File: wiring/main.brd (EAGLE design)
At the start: 75.9 x 73.7 mm, 48 parts, among them IC1 attiny 2313A, J1 J7MM, J11 J7MM, J2 J5MM, J3 J10MM, J4 J7MM, J5 J5MM, J6 J5MM, Q1 12MHz, X1 USB-B

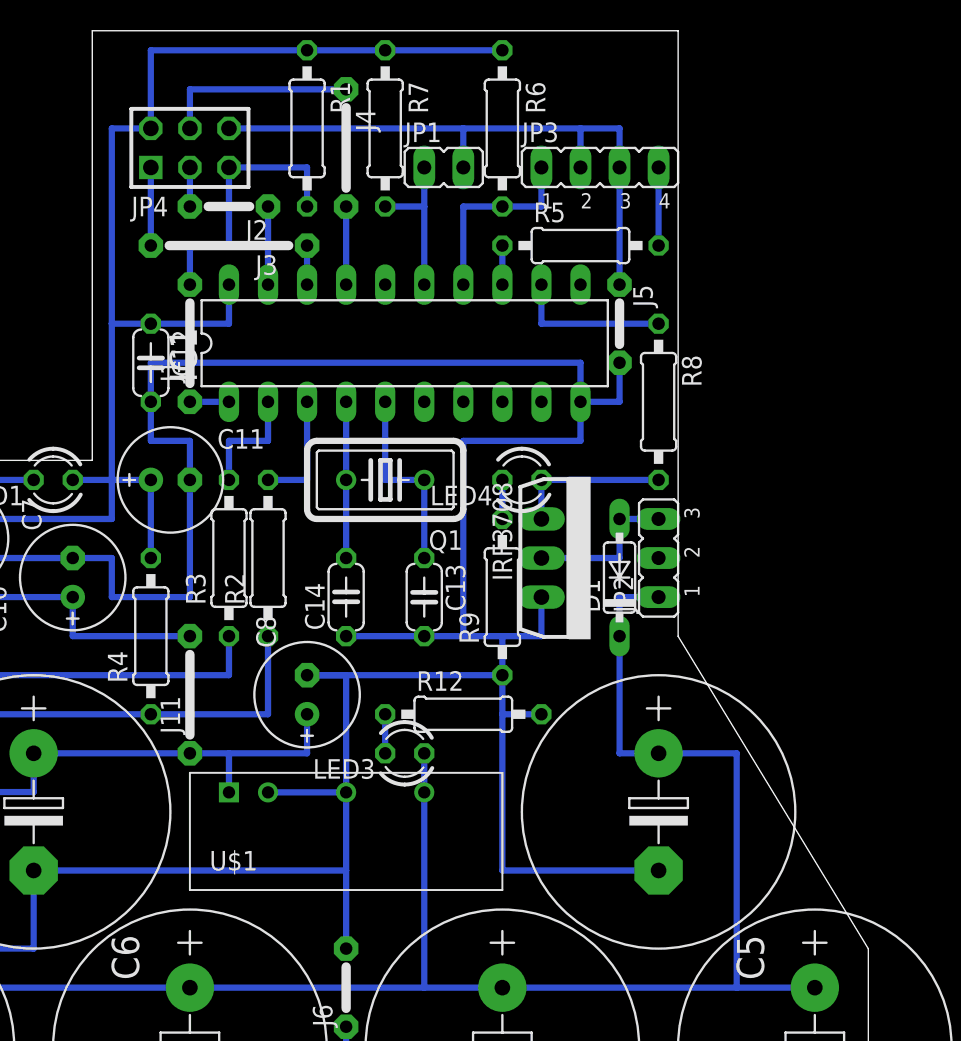
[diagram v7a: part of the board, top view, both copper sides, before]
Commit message: wiring schaltazeige led Widerstand geändert
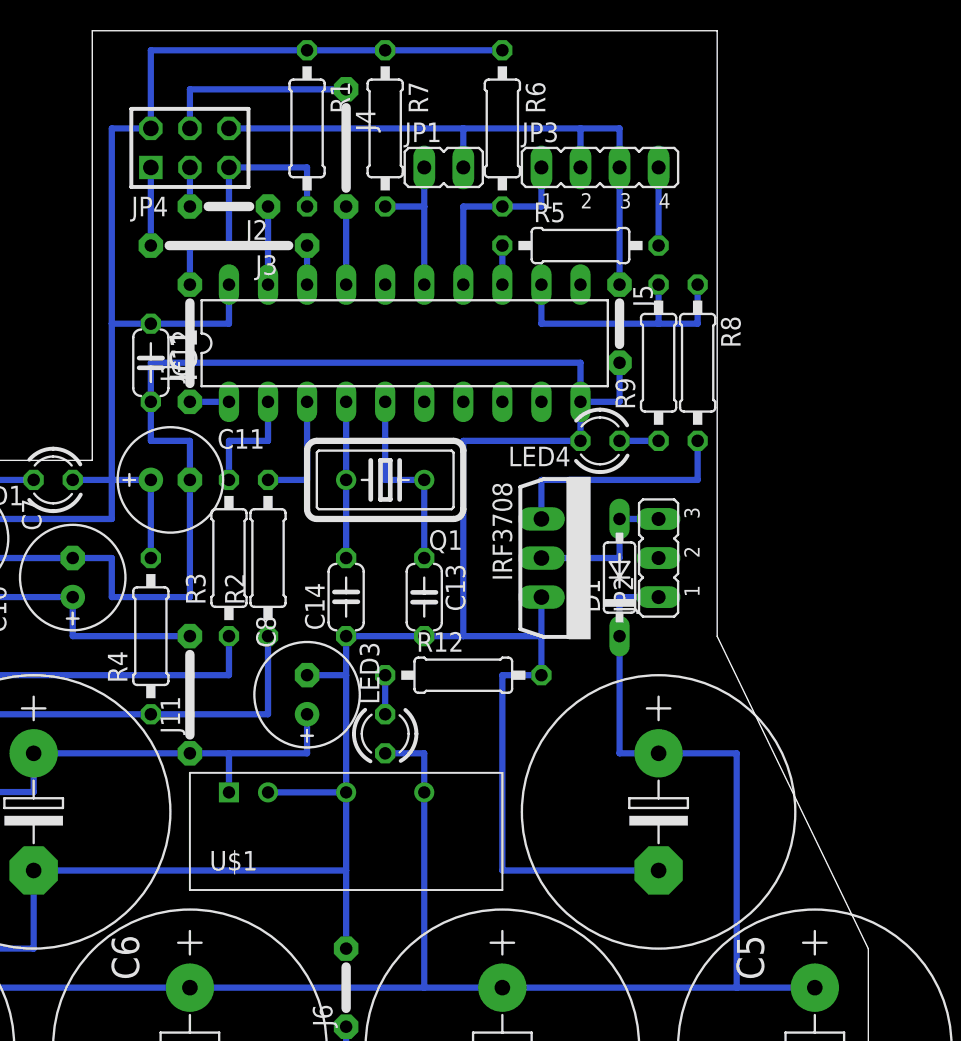
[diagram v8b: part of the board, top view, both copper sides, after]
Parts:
- R9: value 549 -> 649
- moved R9 18.3 mm to (63.5, 53.3)
- moved LED4 5.68 mm to (59.7, 48.3)
- moved R8 3.59 mm to (66.0, 53.3)
- moved R12 2.54 mm to (50.8, 33.0)
- moved LED3 1.80 mm to (45.7, 29.2), turned to 90 degrees
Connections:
- removed net N$6: LED4.K, R9.2
- new net N$7: LED4.A, R9.1
- net GND: now also LED4.K; no longer R9.1
- net N$2: no longer LED4.A
- net PB0: now also R9.2
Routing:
- net GND: track 404.0 -> 393.9 mm
- net PB0: track 10.2 -> 17.8 mm
- net N$2: track 10.2 -> 15.2 mm
- net N$7: track 0.00 -> 2.54 mm
- net N$6: track 2.54 -> 0.00 mm
- net +15V: track 111.8 -> 114.3 mm
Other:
- outline, holes or cut-outs redrawn
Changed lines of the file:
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@@
 <wire x1="1.27" y1="1.27" x2="77.14" y2="1.27" width="0" layer="20"/>
 <wire x1="77.14" y1="1.27" x2="77.14" y2="15.23" width="0" layer="20"/>
-<wire x1="77.14" y1="15.23" x2="64.77" y2="35.55" width="0" layer="20"/>
-<wire x1="64.77" y1="35.55" x2="64.77" y2="74.93" width="0" layer="20"/>
-<wire x1="64.77" y1="74.93" x2="26.67" y2="74.93" width="0" layer="20"/>
+<wire x1="77.14" y1="15.23" x2="67.31" y2="35.55" width="0" layer="20"/>
+<wire x1="67.31" y1="35.55" x2="67.31" y2="74.93" width="0" layer="20"/>
+<wire x1="67.31" y1="74.93" x2="26.67" y2="74.93" width="0" layer="20"/>
 <wire x1="26.67" y1="74.93" x2="26.67" y2="46.99" width="0" layer="20"/>
 <wire x1="26.67" y1="46.99" x2="1.27" y2="46.99" width="0" layer="20"/>
@@
 <element name="C7" library="resistor" package="E2,5-7" value="220µ" x="25.4" y="39.37" rot="R90"/>
 <element name="C10" library="resistor" package="E2,5-7" value="220µ" x="17.78" y="41.91" rot="R270"/>
-<element name="R8" library="rcl" package="0207/10" value="100" x="63.5" y="50.8" rot="R270"/>
+<element name="R8" library="rcl" package="0207/10" value="100" x="66.04" y="53.34" rot="R270"/>
 <element name="R1" library="rcl" package="0207/10" value="10k" x="40.64" y="68.58" rot="R270"/>
 <element name="C13" library="rcl" package="C050-024X044" value="22p" x="48.26" y="38.1" rot="R270"/>
@@
 <element name="D1" library="diode" package="DO35-7" value="1N4148DO35-7" x="60.96" y="39.37" rot="R90"/>
 <element name="IRF3708" library="transistor-power" package="TO262-V" value="IRF3704L-V" x="55.88" y="40.64" rot="R270"/>
-<element name="R9" library="rcl" package="0207/10" value="549" x="53.34" y="38.1" rot="R90"/>
+<element name="R9" library="rcl" package="0207/10" value="649" x="63.5" y="53.34" rot="R90"/>
 <element name="C8" library="resistor" package="E2,5-7" value="220µ" x="40.64" y="31.75" rot="R90"/>
 <element name="U$1" library="eigene" package="SIL7" value="SIM2-0515S" x="35.56" y="25.4"/>
@@
 <element name="LED1" library="led" package="LED3MM" value="" x="24.13" y="45.72" rot="R180"/>
 <element name="LED2" library="led" package="LED3MM" value="" x="11.43" y="20.32" rot="R180"/>
-<element name="LED3" library="led" package="LED3MM" value="LED 3MM 2MA GN" x="46.99" y="27.94" rot="R180"/>
+<element name="LED3" library="led" package="LED3MM" value="LED 3MM 2MA GN" x="45.72" y="29.21" rot="R90"/>
 <element name="R10" library="rcl" package="0207/7" value="649" x="11.43" y="45.72" rot="R180"/>
 <element name="R11" library="rcl" package="0207/7" value="1,5k" x="6.35" y="17.78" rot="R180"/>
-<element name="R12" library="rcl" package="0207/10" value="6,49k" x="50.8" y="30.48"/>
-<element name="LED4" library="led" package="LED3MM" value="" x="54.61" y="45.72" rot="R180"/>
+<element name="R12" library="rcl" package="0207/10" value="6,49k" x="50.8" y="33.02"/>
+<element name="LED4" library="led" package="LED3MM" value="" x="59.69" y="48.26" rot="R180"/>
 </elements>
 <signals>
@@
 <contactref element="R8" pad="2"/>
 <contactref element="IRF3708" pad="1"/>
-<wire x1="55.88" y1="43.18" x2="55.88" y2="45.72" width="0.4064" layer="16"/>
-<wire x1="55.88" y1="45.72" x2="63.5" y2="45.72" width="0.4064" layer="16"/>
-<contactref element="LED4" pad="A"/>
-<wire x1="55.88" y1="45.72" x2="55.88" y2="43.18" width="0" layer="19" extent="1-1"/>
+<wire x1="66.04" y1="48.26" x2="66.04" y2="45.72" width="0.4064" layer="16"/>
+<wire x1="66.04" y1="45.72" x2="55.88" y2="45.72" width="0.4064" layer="16"/>
+<wire x1="55.88" y1="45.72" x2="55.88" y2="43.18" width="0.4064" layer="16"/>
 </signal>
 <signal name="+5V">
@@
 <wire x1="55.88" y1="58.42" x2="55.88" y2="55.88" width="0.4064" layer="16"/>
 <wire x1="55.88" y1="55.88" x2="63.5" y2="55.88" width="0.4064" layer="16"/>
+<wire x1="63.5" y1="55.88" x2="66.04" y2="55.88" width="0.4064" layer="16"/>
+<wire x1="66.04" y1="55.88" x2="66.04" y2="58.42" width="0.4064" layer="16"/>
+<contactref element="R9" pad="2"/>
+<wire x1="63.5" y1="58.42" x2="63.5" y2="55.88" width="0.4064" layer="16"/>
 </signal>
 <signal name="N$18">
@@
 <wire x1="58.42" y1="53.34" x2="58.42" y2="50.8" width="0.4064" layer="16"/>
 <contactref element="IRF3708" pad="3"/>
-<contactref element="R9" pad="1"/>
 <wire x1="7.62" y1="20.32" x2="7.62" y2="15.24" width="0.4064" layer="16"/>
 <wire x1="7.62" y1="15.24" x2="7.62" y2="5.08" width="0.4064" layer="16"/>
-<wire x1="53.34" y1="33.02" x2="53.34" y2="35.56" width="0.4064" layer="16"/>
-<wire x1="53.34" y1="35.56" x2="50.8" y2="35.56" width="0.4064" layer="16"/>
 <wire x1="55.88" y1="38.1" x2="55.88" y2="35.56" width="0.4064" layer="16"/>
-<wire x1="55.88" y1="35.56" x2="53.34" y2="35.56" width="0.4064" layer="16"/>
+<wire x1="55.88" y1="35.56" x2="50.8" y2="35.56" width="0.4064" layer="16"/>
 <contactref element="C8" pad="-"/>
 <contactref element="C1" pad="-"/>
@@
 <contactref element="U$1" pad="PIN4"/>
 <wire x1="63.5" y1="20.32" x2="53.34" y2="20.32" width="0.4064" layer="16"/>
-<wire x1="53.34" y1="20.32" x2="53.34" y2="30.48" width="0.4064" layer="16"/>
-<wire x1="53.34" y1="30.48" x2="53.34" y2="33.02" width="0.4064" layer="16"/>
-<wire x1="40.64" y1="33.02" x2="53.34" y2="33.02" width="0.4064" layer="16"/>
+<wire x1="53.34" y1="20.32" x2="53.34" y2="33.02" width="0.4064" layer="16"/>
 <wire x1="38.1" y1="25.4" x2="43.18" y2="25.4" width="0.4064" layer="16"/>
 <contactref element="J5" pad="1"/>
@@
 <wire x1="2.54" y1="20.32" x2="7.62" y2="20.32" width="0.4064" layer="16"/>
 <wire x1="7.62" y1="20.32" x2="7.62" y2="20.65" width="0.4064" layer="16"/>
-<wire x1="55.88" y1="30.48" x2="53.34" y2="30.48" width="0.4064" layer="16"/>
+<wire x1="55.88" y1="33.02" x2="53.34" y2="33.02" width="0.4064" layer="16"/>
 <wire x1="7.62" y1="45.72" x2="2.54" y2="45.72" width="0.4064" layer="16"/>
 <wire x1="2.54" y1="45.72" x2="2.54" y2="40.64" width="0.4064" layer="16"/>
 <wire x1="22.86" y1="20.32" x2="22.86" y2="15.24" width="0.4064" layer="16"/>
 <wire x1="22.86" y1="15.24" x2="7.62" y2="15.24" width="0.4064" layer="16"/>
+<wire x1="22.86" y1="20.32" x2="43.18" y2="20.32" width="0.4064" layer="16"/>
+<contactref element="LED4" pad="K"/>
 <wire x1="60.96" y1="53.34" x2="60.96" y2="58.42" width="0" layer="19" extent="1-1"/>
-<wire x1="43.18" y1="25.4" x2="43.18" y2="33.02" width="0" layer="19" extent="16-16"/>
-<wire x1="22.86" y1="20.32" x2="43.18" y2="20.32" width="0.4064" layer="16"/>
+<wire x1="58.42" y1="48.26" x2="50.8" y2="48.26" width="0" layer="19" extent="16-16"/>
+<wire x1="43.18" y1="25.4" x2="43.18" y2="20.32" width="0" layer="19" extent="16-16"/>
+<wire x1="43.18" y1="35.56" x2="43.18" y2="33.02" width="0.4064" layer="16"/>
+<wire x1="55.88" y1="33.02" x2="55.88" y2="35.56" width="0.4064" layer="16"/>
 </signal>
 <signal name="SCK">
@@
 <contactref element="LED3" pad="A"/>
 <wire x1="48.26" y1="25.4" x2="48.26" y2="27.94" width="0.4064" layer="16"/>
+<wire x1="48.26" y1="27.94" x2="45.72" y2="27.94" width="0.4064" layer="16"/>
 </signal>
 <signal name="D-">
@@
 <contactref element="LED3" pad="K"/>
 <contactref element="R12" pad="1"/>
-<wire x1="45.72" y1="27.94" x2="45.72" y2="30.48" width="0.4064" layer="16"/>
+<wire x1="45.72" y1="30.48" x2="45.72" y2="33.02" width="0.4064" layer="16"/>
 </signal>
 <signal name="N$4">
@@
 <wire x1="45.72" y1="73.66" x2="40.64" y2="73.66" width="0" layer="19" extent="1-1"/>
 </signal>
-<signal name="N$6">
-<contactref element="R9" pad="2"/>
-<contactref element="LED4" pad="K"/>
-<wire x1="53.34" y1="43.18" x2="53.34" y2="45.72" width="0.4064" layer="16"/>
+<signal name="N$7">
+<contactref element="R9" pad="1"/>
+<contactref element="LED4" pad="A"/>
+<wire x1="63.5" y1="48.26" x2="60.96" y2="48.26" width="0.4064" layer="16"/>
 </signal>
 </signals>
-<errors>
-</errors>
 </board>
 </drawing>
